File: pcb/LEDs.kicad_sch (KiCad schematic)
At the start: 66 parts, among them U76 74AHCT125

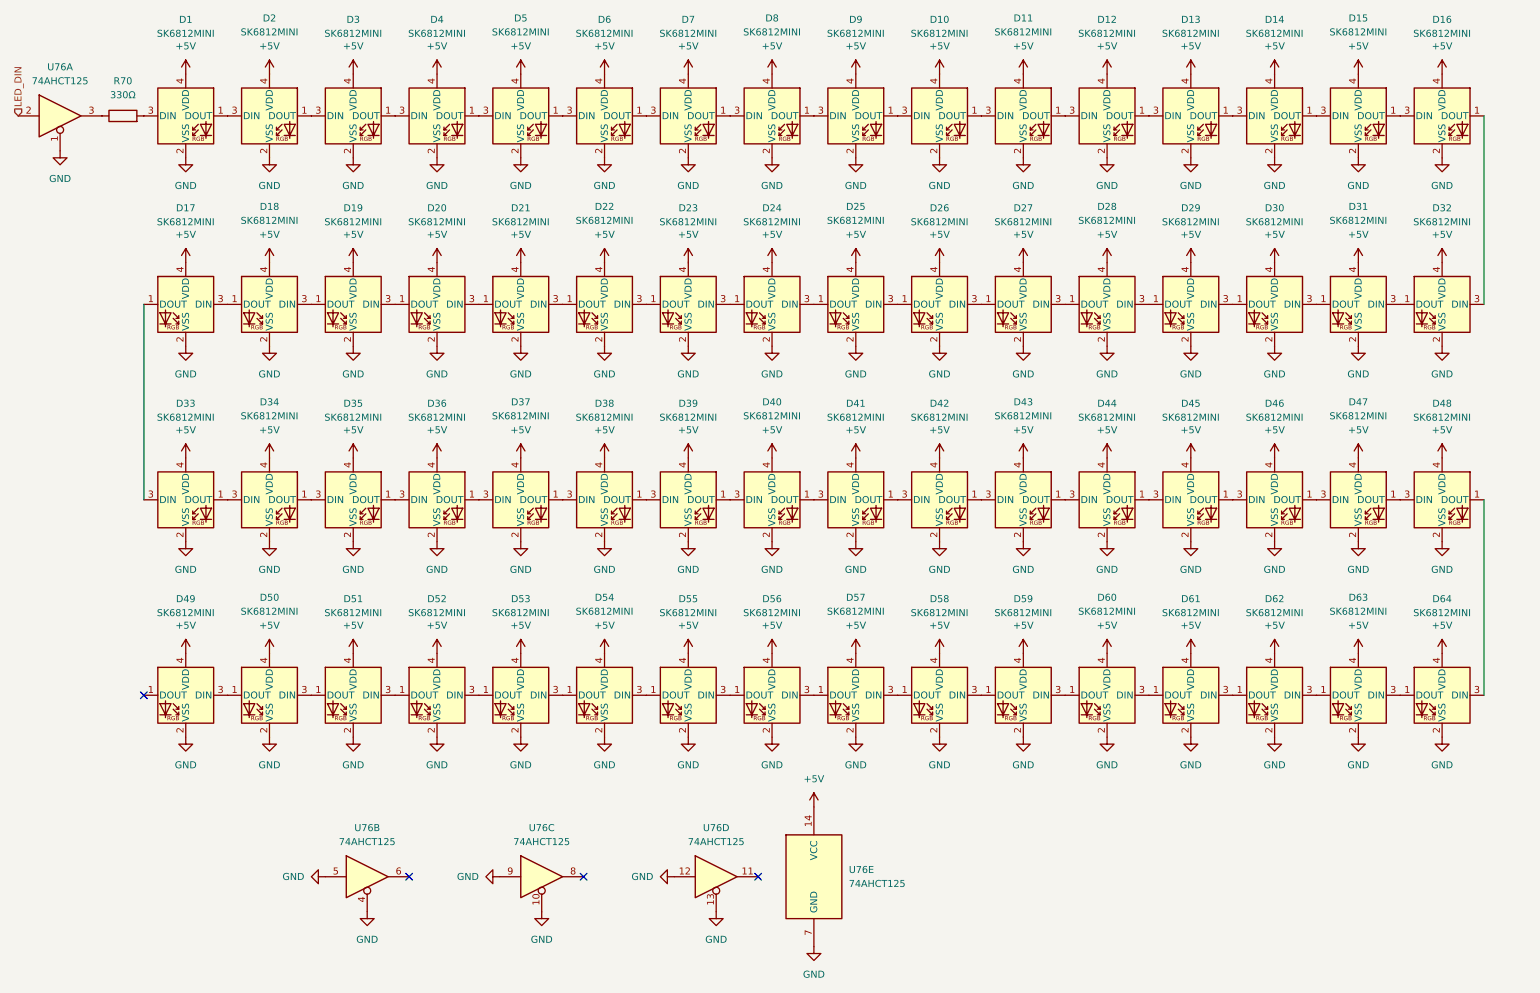
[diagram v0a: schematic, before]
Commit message: feat: completed layout for a single switch
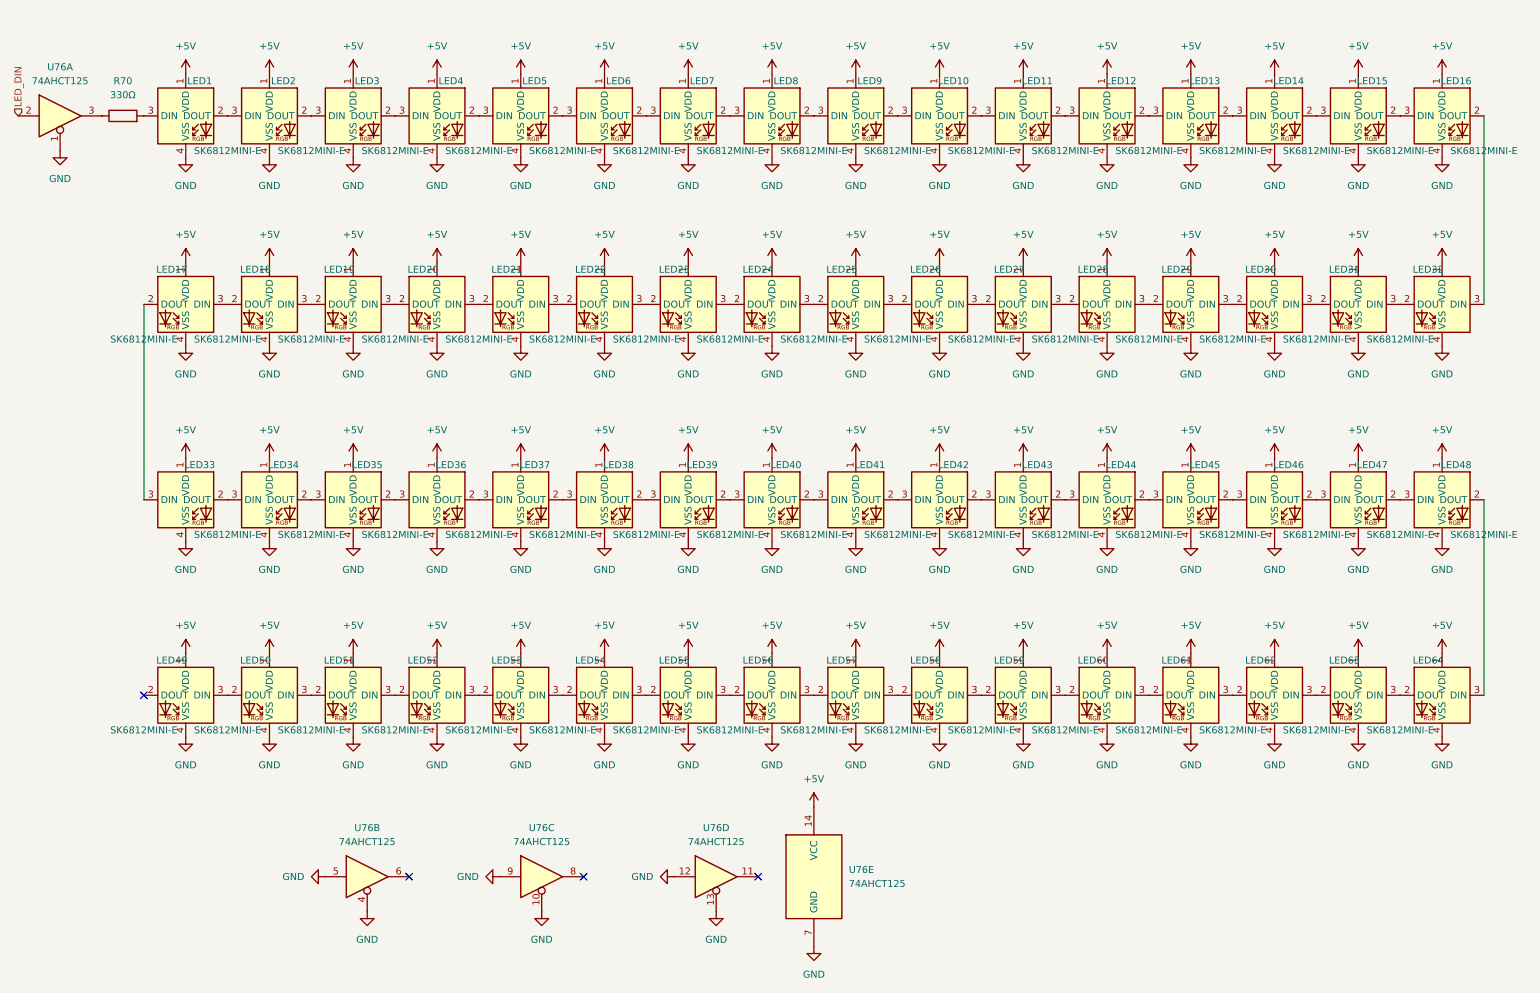
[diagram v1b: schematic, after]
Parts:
- LED1: renamed from D1; value SK6812MINI -> SK6812MINI-E; footprint LED_SMD:LED_SK6812MINI_PLCC4_3.5x3.5mm_P1.75mm -> PCM_marbastlib-various:LED_6028R; symbol LED:SK6812MINI -> PCM_marbastlib-various:SK6812MINI-E
- LED10: renamed from D10; value SK6812MINI -> SK6812MINI-E; footprint LED_SMD:LED_SK6812MINI_PLCC4_3.5x3.5mm_P1.75mm -> PCM_marbastlib-various:LED_6028R; symbol LED:SK6812MINI -> PCM_marbastlib-various:SK6812MINI-E
- LED11: renamed from D11; value SK6812MINI -> SK6812MINI-E; footprint LED_SMD:LED_SK6812MINI_PLCC4_3.5x3.5mm_P1.75mm -> PCM_marbastlib-various:LED_6028R; symbol LED:SK6812MINI -> PCM_marbastlib-various:SK6812MINI-E
- LED12: renamed from D12; value SK6812MINI -> SK6812MINI-E; footprint LED_SMD:LED_SK6812MINI_PLCC4_3.5x3.5mm_P1.75mm -> PCM_marbastlib-various:LED_6028R; symbol LED:SK6812MINI -> PCM_marbastlib-various:SK6812MINI-E
- LED13: renamed from D13; value SK6812MINI -> SK6812MINI-E; footprint LED_SMD:LED_SK6812MINI_PLCC4_3.5x3.5mm_P1.75mm -> PCM_marbastlib-various:LED_6028R; symbol LED:SK6812MINI -> PCM_marbastlib-various:SK6812MINI-E
- LED14: renamed from D14; value SK6812MINI -> SK6812MINI-E; footprint LED_SMD:LED_SK6812MINI_PLCC4_3.5x3.5mm_P1.75mm -> PCM_marbastlib-various:LED_6028R; symbol LED:SK6812MINI -> PCM_marbastlib-various:SK6812MINI-E
- LED15: renamed from D15; value SK6812MINI -> SK6812MINI-E; footprint LED_SMD:LED_SK6812MINI_PLCC4_3.5x3.5mm_P1.75mm -> PCM_marbastlib-various:LED_6028R; symbol LED:SK6812MINI -> PCM_marbastlib-various:SK6812MINI-E
- LED16: renamed from D16; value SK6812MINI -> SK6812MINI-E; footprint LED_SMD:LED_SK6812MINI_PLCC4_3.5x3.5mm_P1.75mm -> PCM_marbastlib-various:LED_6028R; symbol LED:SK6812MINI -> PCM_marbastlib-various:SK6812MINI-E
- LED17: renamed from D17; value SK6812MINI -> SK6812MINI-E; footprint LED_SMD:LED_SK6812MINI_PLCC4_3.5x3.5mm_P1.75mm -> PCM_marbastlib-various:LED_6028R; symbol LED:SK6812MINI -> PCM_marbastlib-various:SK6812MINI-E
- LED18: renamed from D18; value SK6812MINI -> SK6812MINI-E; footprint LED_SMD:LED_SK6812MINI_PLCC4_3.5x3.5mm_P1.75mm -> PCM_marbastlib-various:LED_6028R; symbol LED:SK6812MINI -> PCM_marbastlib-various:SK6812MINI-E
- LED19: renamed from D19; value SK6812MINI -> SK6812MINI-E; footprint LED_SMD:LED_SK6812MINI_PLCC4_3.5x3.5mm_P1.75mm -> PCM_marbastlib-various:LED_6028R; symbol LED:SK6812MINI -> PCM_marbastlib-various:SK6812MINI-E
- LED2: renamed from D2; value SK6812MINI -> SK6812MINI-E; footprint LED_SMD:LED_SK6812MINI_PLCC4_3.5x3.5mm_P1.75mm -> PCM_marbastlib-various:LED_6028R; symbol LED:SK6812MINI -> PCM_marbastlib-various:SK6812MINI-E
- LED20: renamed from D20; value SK6812MINI -> SK6812MINI-E; footprint LED_SMD:LED_SK6812MINI_PLCC4_3.5x3.5mm_P1.75mm -> PCM_marbastlib-various:LED_6028R; symbol LED:SK6812MINI -> PCM_marbastlib-various:SK6812MINI-E
- LED21: renamed from D21; value SK6812MINI -> SK6812MINI-E; footprint LED_SMD:LED_SK6812MINI_PLCC4_3.5x3.5mm_P1.75mm -> PCM_marbastlib-various:LED_6028R; symbol LED:SK6812MINI -> PCM_marbastlib-various:SK6812MINI-E
- LED22: renamed from D22; value SK6812MINI -> SK6812MINI-E; footprint LED_SMD:LED_SK6812MINI_PLCC4_3.5x3.5mm_P1.75mm -> PCM_marbastlib-various:LED_6028R; symbol LED:SK6812MINI -> PCM_marbastlib-various:SK6812MINI-E
- LED23: renamed from D23; value SK6812MINI -> SK6812MINI-E; footprint LED_SMD:LED_SK6812MINI_PLCC4_3.5x3.5mm_P1.75mm -> PCM_marbastlib-various:LED_6028R; symbol LED:SK6812MINI -> PCM_marbastlib-various:SK6812MINI-E
- LED24: renamed from D24; value SK6812MINI -> SK6812MINI-E; footprint LED_SMD:LED_SK6812MINI_PLCC4_3.5x3.5mm_P1.75mm -> PCM_marbastlib-various:LED_6028R; symbol LED:SK6812MINI -> PCM_marbastlib-various:SK6812MINI-E
- LED25: renamed from D25; value SK6812MINI -> SK6812MINI-E; footprint LED_SMD:LED_SK6812MINI_PLCC4_3.5x3.5mm_P1.75mm -> PCM_marbastlib-various:LED_6028R; symbol LED:SK6812MINI -> PCM_marbastlib-various:SK6812MINI-E
- LED26: renamed from D26; value SK6812MINI -> SK6812MINI-E; footprint LED_SMD:LED_SK6812MINI_PLCC4_3.5x3.5mm_P1.75mm -> PCM_marbastlib-various:LED_6028R; symbol LED:SK6812MINI -> PCM_marbastlib-various:SK6812MINI-E
- LED27: renamed from D27; value SK6812MINI -> SK6812MINI-E; footprint LED_SMD:LED_SK6812MINI_PLCC4_3.5x3.5mm_P1.75mm -> PCM_marbastlib-various:LED_6028R; symbol LED:SK6812MINI -> PCM_marbastlib-various:SK6812MINI-E
- LED28: renamed from D28; value SK6812MINI -> SK6812MINI-E; footprint LED_SMD:LED_SK6812MINI_PLCC4_3.5x3.5mm_P1.75mm -> PCM_marbastlib-various:LED_6028R; symbol LED:SK6812MINI -> PCM_marbastlib-various:SK6812MINI-E
- LED29: renamed from D29; value SK6812MINI -> SK6812MINI-E; footprint LED_SMD:LED_SK6812MINI_PLCC4_3.5x3.5mm_P1.75mm -> PCM_marbastlib-various:LED_6028R; symbol LED:SK6812MINI -> PCM_marbastlib-various:SK6812MINI-E
- LED3: renamed from D3; value SK6812MINI -> SK6812MINI-E; footprint LED_SMD:LED_SK6812MINI_PLCC4_3.5x3.5mm_P1.75mm -> PCM_marbastlib-various:LED_6028R; symbol LED:SK6812MINI -> PCM_marbastlib-various:SK6812MINI-E
- LED30: renamed from D30; value SK6812MINI -> SK6812MINI-E; footprint LED_SMD:LED_SK6812MINI_PLCC4_3.5x3.5mm_P1.75mm -> PCM_marbastlib-various:LED_6028R; symbol LED:SK6812MINI -> PCM_marbastlib-various:SK6812MINI-E
- LED31: renamed from D31; value SK6812MINI -> SK6812MINI-E; footprint LED_SMD:LED_SK6812MINI_PLCC4_3.5x3.5mm_P1.75mm -> PCM_marbastlib-various:LED_6028R; symbol LED:SK6812MINI -> PCM_marbastlib-various:SK6812MINI-E
- LED32: renamed from D32; value SK6812MINI -> SK6812MINI-E; footprint LED_SMD:LED_SK6812MINI_PLCC4_3.5x3.5mm_P1.75mm -> PCM_marbastlib-various:LED_6028R; symbol LED:SK6812MINI -> PCM_marbastlib-various:SK6812MINI-E
- LED33: renamed from D33; value SK6812MINI -> SK6812MINI-E; footprint LED_SMD:LED_SK6812MINI_PLCC4_3.5x3.5mm_P1.75mm -> PCM_marbastlib-various:LED_6028R; symbol LED:SK6812MINI -> PCM_marbastlib-various:SK6812MINI-E
- LED34: renamed from D34; value SK6812MINI -> SK6812MINI-E; footprint LED_SMD:LED_SK6812MINI_PLCC4_3.5x3.5mm_P1.75mm -> PCM_marbastlib-various:LED_6028R; symbol LED:SK6812MINI -> PCM_marbastlib-various:SK6812MINI-E
- LED35: renamed from D35; value SK6812MINI -> SK6812MINI-E; footprint LED_SMD:LED_SK6812MINI_PLCC4_3.5x3.5mm_P1.75mm -> PCM_marbastlib-various:LED_6028R; symbol LED:SK6812MINI -> PCM_marbastlib-various:SK6812MINI-E
- LED36: renamed from D36; value SK6812MINI -> SK6812MINI-E; footprint LED_SMD:LED_SK6812MINI_PLCC4_3.5x3.5mm_P1.75mm -> PCM_marbastlib-various:LED_6028R; symbol LED:SK6812MINI -> PCM_marbastlib-various:SK6812MINI-E
- LED37: renamed from D37; value SK6812MINI -> SK6812MINI-E; footprint LED_SMD:LED_SK6812MINI_PLCC4_3.5x3.5mm_P1.75mm -> PCM_marbastlib-various:LED_6028R; symbol LED:SK6812MINI -> PCM_marbastlib-various:SK6812MINI-E
- LED38: renamed from D38; value SK6812MINI -> SK6812MINI-E; footprint LED_SMD:LED_SK6812MINI_PLCC4_3.5x3.5mm_P1.75mm -> PCM_marbastlib-various:LED_6028R; symbol LED:SK6812MINI -> PCM_marbastlib-various:SK6812MINI-E
- LED39: renamed from D39; value SK6812MINI -> SK6812MINI-E; footprint LED_SMD:LED_SK6812MINI_PLCC4_3.5x3.5mm_P1.75mm -> PCM_marbastlib-various:LED_6028R; symbol LED:SK6812MINI -> PCM_marbastlib-various:SK6812MINI-E
- LED4: renamed from D4; value SK6812MINI -> SK6812MINI-E; footprint LED_SMD:LED_SK6812MINI_PLCC4_3.5x3.5mm_P1.75mm -> PCM_marbastlib-various:LED_6028R; symbol LED:SK6812MINI -> PCM_marbastlib-various:SK6812MINI-E
- LED40: renamed from D40; value SK6812MINI -> SK6812MINI-E; footprint LED_SMD:LED_SK6812MINI_PLCC4_3.5x3.5mm_P1.75mm -> PCM_marbastlib-various:LED_6028R; symbol LED:SK6812MINI -> PCM_marbastlib-various:SK6812MINI-E
- LED41: renamed from D41; value SK6812MINI -> SK6812MINI-E; footprint LED_SMD:LED_SK6812MINI_PLCC4_3.5x3.5mm_P1.75mm -> PCM_marbastlib-various:LED_6028R; symbol LED:SK6812MINI -> PCM_marbastlib-various:SK6812MINI-E
- LED42: renamed from D42; value SK6812MINI -> SK6812MINI-E; footprint LED_SMD:LED_SK6812MINI_PLCC4_3.5x3.5mm_P1.75mm -> PCM_marbastlib-various:LED_6028R; symbol LED:SK6812MINI -> PCM_marbastlib-various:SK6812MINI-E
- LED43: renamed from D43; value SK6812MINI -> SK6812MINI-E; footprint LED_SMD:LED_SK6812MINI_PLCC4_3.5x3.5mm_P1.75mm -> PCM_marbastlib-various:LED_6028R; symbol LED:SK6812MINI -> PCM_marbastlib-various:SK6812MINI-E
- LED44: renamed from D44; value SK6812MINI -> SK6812MINI-E; footprint LED_SMD:LED_SK6812MINI_PLCC4_3.5x3.5mm_P1.75mm -> PCM_marbastlib-various:LED_6028R; symbol LED:SK6812MINI -> PCM_marbastlib-various:SK6812MINI-E
- LED45: renamed from D45; value SK6812MINI -> SK6812MINI-E; footprint LED_SMD:LED_SK6812MINI_PLCC4_3.5x3.5mm_P1.75mm -> PCM_marbastlib-various:LED_6028R; symbol LED:SK6812MINI -> PCM_marbastlib-various:SK6812MINI-E
- LED46: renamed from D46; value SK6812MINI -> SK6812MINI-E; footprint LED_SMD:LED_SK6812MINI_PLCC4_3.5x3.5mm_P1.75mm -> PCM_marbastlib-various:LED_6028R; symbol LED:SK6812MINI -> PCM_marbastlib-various:SK6812MINI-E
- LED47: renamed from D47; value SK6812MINI -> SK6812MINI-E; footprint LED_SMD:LED_SK6812MINI_PLCC4_3.5x3.5mm_P1.75mm -> PCM_marbastlib-various:LED_6028R; symbol LED:SK6812MINI -> PCM_marbastlib-various:SK6812MINI-E
- LED48: renamed from D48; value SK6812MINI -> SK6812MINI-E; footprint LED_SMD:LED_SK6812MINI_PLCC4_3.5x3.5mm_P1.75mm -> PCM_marbastlib-various:LED_6028R; symbol LED:SK6812MINI -> PCM_marbastlib-various:SK6812MINI-E
- LED49: renamed from D49; value SK6812MINI -> SK6812MINI-E; footprint LED_SMD:LED_SK6812MINI_PLCC4_3.5x3.5mm_P1.75mm -> PCM_marbastlib-various:LED_6028R; symbol LED:SK6812MINI -> PCM_marbastlib-various:SK6812MINI-E
- LED5: renamed from D5; value SK6812MINI -> SK6812MINI-E; footprint LED_SMD:LED_SK6812MINI_PLCC4_3.5x3.5mm_P1.75mm -> PCM_marbastlib-various:LED_6028R; symbol LED:SK6812MINI -> PCM_marbastlib-various:SK6812MINI-E
- LED50: renamed from D50; value SK6812MINI -> SK6812MINI-E; footprint LED_SMD:LED_SK6812MINI_PLCC4_3.5x3.5mm_P1.75mm -> PCM_marbastlib-various:LED_6028R; symbol LED:SK6812MINI -> PCM_marbastlib-various:SK6812MINI-E
- LED51: renamed from D51; value SK6812MINI -> SK6812MINI-E; footprint LED_SMD:LED_SK6812MINI_PLCC4_3.5x3.5mm_P1.75mm -> PCM_marbastlib-various:LED_6028R; symbol LED:SK6812MINI -> PCM_marbastlib-various:SK6812MINI-E
- LED52: renamed from D52; value SK6812MINI -> SK6812MINI-E; footprint LED_SMD:LED_SK6812MINI_PLCC4_3.5x3.5mm_P1.75mm -> PCM_marbastlib-various:LED_6028R; symbol LED:SK6812MINI -> PCM_marbastlib-various:SK6812MINI-E
- LED53: renamed from D53; value SK6812MINI -> SK6812MINI-E; footprint LED_SMD:LED_SK6812MINI_PLCC4_3.5x3.5mm_P1.75mm -> PCM_marbastlib-various:LED_6028R; symbol LED:SK6812MINI -> PCM_marbastlib-various:SK6812MINI-E
- LED54: renamed from D54; value SK6812MINI -> SK6812MINI-E; footprint LED_SMD:LED_SK6812MINI_PLCC4_3.5x3.5mm_P1.75mm -> PCM_marbastlib-various:LED_6028R; symbol LED:SK6812MINI -> PCM_marbastlib-various:SK6812MINI-E
- LED55: renamed from D55; value SK6812MINI -> SK6812MINI-E; footprint LED_SMD:LED_SK6812MINI_PLCC4_3.5x3.5mm_P1.75mm -> PCM_marbastlib-various:LED_6028R; symbol LED:SK6812MINI -> PCM_marbastlib-various:SK6812MINI-E
- LED56: renamed from D56; value SK6812MINI -> SK6812MINI-E; footprint LED_SMD:LED_SK6812MINI_PLCC4_3.5x3.5mm_P1.75mm -> PCM_marbastlib-various:LED_6028R; symbol LED:SK6812MINI -> PCM_marbastlib-various:SK6812MINI-E
- LED57: renamed from D57; value SK6812MINI -> SK6812MINI-E; footprint LED_SMD:LED_SK6812MINI_PLCC4_3.5x3.5mm_P1.75mm -> PCM_marbastlib-various:LED_6028R; symbol LED:SK6812MINI -> PCM_marbastlib-various:SK6812MINI-E
- LED58: renamed from D58; value SK6812MINI -> SK6812MINI-E; footprint LED_SMD:LED_SK6812MINI_PLCC4_3.5x3.5mm_P1.75mm -> PCM_marbastlib-various:LED_6028R; symbol LED:SK6812MINI -> PCM_marbastlib-various:SK6812MINI-E
- LED59: renamed from D59; value SK6812MINI -> SK6812MINI-E; footprint LED_SMD:LED_SK6812MINI_PLCC4_3.5x3.5mm_P1.75mm -> PCM_marbastlib-various:LED_6028R; symbol LED:SK6812MINI -> PCM_marbastlib-various:SK6812MINI-E
- LED6: renamed from D6; value SK6812MINI -> SK6812MINI-E; footprint LED_SMD:LED_SK6812MINI_PLCC4_3.5x3.5mm_P1.75mm -> PCM_marbastlib-various:LED_6028R; symbol LED:SK6812MINI -> PCM_marbastlib-various:SK6812MINI-E
- LED60: renamed from D60; value SK6812MINI -> SK6812MINI-E; footprint LED_SMD:LED_SK6812MINI_PLCC4_3.5x3.5mm_P1.75mm -> PCM_marbastlib-various:LED_6028R; symbol LED:SK6812MINI -> PCM_marbastlib-various:SK6812MINI-E
- LED61: renamed from D61; value SK6812MINI -> SK6812MINI-E; footprint LED_SMD:LED_SK6812MINI_PLCC4_3.5x3.5mm_P1.75mm -> PCM_marbastlib-various:LED_6028R; symbol LED:SK6812MINI -> PCM_marbastlib-various:SK6812MINI-E
- LED62: renamed from D62; value SK6812MINI -> SK6812MINI-E; footprint LED_SMD:LED_SK6812MINI_PLCC4_3.5x3.5mm_P1.75mm -> PCM_marbastlib-various:LED_6028R; symbol LED:SK6812MINI -> PCM_marbastlib-various:SK6812MINI-E
- LED63: renamed from D63; value SK6812MINI -> SK6812MINI-E; footprint LED_SMD:LED_SK6812MINI_PLCC4_3.5x3.5mm_P1.75mm -> PCM_marbastlib-various:LED_6028R; symbol LED:SK6812MINI -> PCM_marbastlib-various:SK6812MINI-E
- LED64: renamed from D64; value SK6812MINI -> SK6812MINI-E; footprint LED_SMD:LED_SK6812MINI_PLCC4_3.5x3.5mm_P1.75mm -> PCM_marbastlib-various:LED_6028R; symbol LED:SK6812MINI -> PCM_marbastlib-various:SK6812MINI-E
- LED7: renamed from D7; value SK6812MINI -> SK6812MINI-E; footprint LED_SMD:LED_SK6812MINI_PLCC4_3.5x3.5mm_P1.75mm -> PCM_marbastlib-various:LED_6028R; symbol LED:SK6812MINI -> PCM_marbastlib-various:SK6812MINI-E
- LED8: renamed from D8; value SK6812MINI -> SK6812MINI-E; footprint LED_SMD:LED_SK6812MINI_PLCC4_3.5x3.5mm_P1.75mm -> PCM_marbastlib-various:LED_6028R; symbol LED:SK6812MINI -> PCM_marbastlib-various:SK6812MINI-E
- LED9: renamed from D9; value SK6812MINI -> SK6812MINI-E; footprint LED_SMD:LED_SK6812MINI_PLCC4_3.5x3.5mm_P1.75mm -> PCM_marbastlib-various:LED_6028R; symbol LED:SK6812MINI -> PCM_marbastlib-various:SK6812MINI-E
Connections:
- net +5V: now also LED1.1 (VDD), LED10.1 (VDD), LED11.1 (VDD), LED12.1 (VDD), LED13.1 (VDD), LED14.1 (VDD), LED15.1 (VDD), LED16.1 (VDD), LED17.1 (VDD), LED18.1 (VDD), LED19.1 (VDD), LED2.1 (VDD), LED20.1 (VDD), LED21.1 (VDD), LED22.1 (VDD), LED23.1 (VDD), LED24.1 (VDD), LED25.1 (VDD), LED26.1 (VDD), LED27.1 (VDD), LED28.1 (VDD), LED29.1 (VDD), LED3.1 (VDD), LED30.1 (VDD), LED31.1 (VDD), LED32.1 (VDD), LED33.1 (VDD), LED34.1 (VDD), LED35.1 (VDD), LED36.1 (VDD), LED37.1 (VDD), LED38.1 (VDD), LED39.1 (VDD), LED4.1 (VDD), LED40.1 (VDD), LED41.1 (VDD), LED42.1 (VDD), LED43.1 (VDD), LED44.1 (VDD), LED45.1 (VDD), LED46.1 (VDD), LED47.1 (VDD), LED48.1 (VDD), LED49.1 (VDD), LED5.1 (VDD), LED50.1 (VDD), LED51.1 (VDD), LED52.1 (VDD), LED53.1 (VDD), LED54.1 (VDD), LED55.1 (VDD), LED56.1 (VDD), LED57.1 (VDD), LED58.1 (VDD), LED59.1 (VDD), LED6.1 (VDD), LED60.1 (VDD), LED61.1 (VDD), LED62.1 (VDD), LED63.1 (VDD), LED64.1 (VDD), LED7.1 (VDD), LED8.1 (VDD), LED9.1 (VDD); no longer LED1.4 (VDD), LED10.4 (VDD), LED11.4 (VDD), LED12.4 (VDD), LED13.4 (VDD), LED14.4 (VDD), LED15.4 (VDD), LED16.4 (VDD), LED17.4 (VDD), LED18.4 (VDD), LED19.4 (VDD), LED2.4 (VDD), LED20.4 (VDD), LED21.4 (VDD), LED22.4 (VDD), LED23.4 (VDD), LED24.4 (VDD), LED25.4 (VDD), LED26.4 (VDD), LED27.4 (VDD), LED28.4 (VDD), LED29.4 (VDD), LED3.4 (VDD), LED30.4 (VDD), LED31.4 (VDD), LED32.4 (VDD), LED33.4 (VDD), LED34.4 (VDD), LED35.4 (VDD), LED36.4 (VDD), LED37.4 (VDD), LED38.4 (VDD), LED39.4 (VDD), LED4.4 (VDD), LED40.4 (VDD), LED41.4 (VDD), LED42.4 (VDD), LED43.4 (VDD), LED44.4 (VDD), LED45.4 (VDD), LED46.4 (VDD), LED47.4 (VDD), LED48.4 (VDD), LED49.4 (VDD), LED5.4 (VDD), LED50.4 (VDD), LED51.4 (VDD), LED52.4 (VDD), LED53.4 (VDD), LED54.4 (VDD), LED55.4 (VDD), LED56.4 (VDD), LED57.4 (VDD), LED58.4 (VDD), LED59.4 (VDD), LED6.4 (VDD), LED60.4 (VDD), LED61.4 (VDD), LED62.4 (VDD), LED63.4 (VDD), LED64.4 (VDD), LED7.4 (VDD), LED8.4 (VDD), LED9.4 (VDD)
- net GND: now also LED1.4 (VSS), LED10.4 (VSS), LED11.4 (VSS), LED12.4 (VSS), LED13.4 (VSS), LED14.4 (VSS), LED15.4 (VSS), LED16.4 (VSS), LED17.4 (VSS), LED18.4 (VSS), LED19.4 (VSS), LED2.4 (VSS), LED20.4 (VSS), LED21.4 (VSS), LED22.4 (VSS), LED23.4 (VSS), LED24.4 (VSS), LED25.4 (VSS), LED26.4 (VSS), LED27.4 (VSS), LED28.4 (VSS), LED29.4 (VSS), LED3.4 (VSS), LED30.4 (VSS), LED31.4 (VSS), LED32.4 (VSS), LED33.4 (VSS), LED34.4 (VSS), LED35.4 (VSS), LED36.4 (VSS), LED37.4 (VSS), LED38.4 (VSS), LED39.4 (VSS), LED4.4 (VSS), LED40.4 (VSS), LED41.4 (VSS), LED42.4 (VSS), LED43.4 (VSS), LED44.4 (VSS), LED45.4 (VSS), LED46.4 (VSS), LED47.4 (VSS), LED48.4 (VSS), LED49.4 (VSS), LED5.4 (VSS), LED50.4 (VSS), LED51.4 (VSS), LED52.4 (VSS), LED53.4 (VSS), LED54.4 (VSS), LED55.4 (VSS), LED56.4 (VSS), LED57.4 (VSS), LED58.4 (VSS), LED59.4 (VSS), LED6.4 (VSS), LED60.4 (VSS), LED61.4 (VSS), LED62.4 (VSS), LED63.4 (VSS), LED64.4 (VSS), LED7.4 (VSS), LED8.4 (VSS), LED9.4 (VSS); no longer LED1.2 (VSS), LED10.2 (VSS), LED11.2 (VSS), LED12.2 (VSS), LED13.2 (VSS), LED14.2 (VSS), LED15.2 (VSS), LED16.2 (VSS), LED17.2 (VSS), LED18.2 (VSS), LED19.2 (VSS), LED2.2 (VSS), LED20.2 (VSS), LED21.2 (VSS), LED22.2 (VSS), LED23.2 (VSS), LED24.2 (VSS), LED25.2 (VSS), LED26.2 (VSS), LED27.2 (VSS), LED28.2 (VSS), LED29.2 (VSS), LED3.2 (VSS), LED30.2 (VSS), LED31.2 (VSS), LED32.2 (VSS), LED33.2 (VSS), LED34.2 (VSS), LED35.2 (VSS), LED36.2 (VSS), LED37.2 (VSS), LED38.2 (VSS), LED39.2 (VSS), LED4.2 (VSS), LED40.2 (VSS), LED41.2 (VSS), LED42.2 (VSS), LED43.2 (VSS), LED44.2 (VSS), LED45.2 (VSS), LED46.2 (VSS), LED47.2 (VSS), LED48.2 (VSS), LED49.2 (VSS), LED5.2 (VSS), LED50.2 (VSS), LED51.2 (VSS), LED52.2 (VSS), LED53.2 (VSS), LED54.2 (VSS), LED55.2 (VSS), LED56.2 (VSS), LED57.2 (VSS), LED58.2 (VSS), LED59.2 (VSS), LED6.2 (VSS), LED60.2 (VSS), LED61.2 (VSS), LED62.2 (VSS), LED63.2 (VSS), LED64.2 (VSS), LED7.2 (VSS), LED8.2 (VSS), LED9.2 (VSS)
- net at LED4.3 (DIN): now also LED3.2 (DOUT); no longer LED3.1 (DOUT)
- net at LED3.3 (DIN): now also LED2.2 (DOUT); no longer LED2.1 (DOUT)
- net at LED49.3 (DIN): now also LED50.2 (DOUT); no longer LED50.1 (DOUT)
- net at LED50.3 (DIN): now also LED51.2 (DOUT); no longer LED51.1 (DOUT)
- net at LED8.3 (DIN): now also LED7.2 (DOUT); no longer LED7.1 (DOUT)
- net at LED7.3 (DIN): now also LED6.2 (DOUT); no longer LED6.1 (DOUT)
- net at LED64.3 (DIN): now also LED48.2 (DOUT); no longer LED48.1 (DOUT)
- net at LED48.3 (DIN): now also LED47.2 (DOUT); no longer LED47.1 (DOUT)
- net at LED6.3 (DIN): now also LED5.2 (DOUT); no longer LED5.1 (DOUT)
- net at LED5.3 (DIN): now also LED4.2 (DOUT); no longer LED4.1 (DOUT)
- net at LED56.3 (DIN): now also LED57.2 (DOUT); no longer LED57.1 (DOUT)
- net at LED57.3 (DIN): now also LED58.2 (DOUT); no longer LED58.1 (DOUT)
- net at LED28.3 (DIN): now also LED29.2 (DOUT); no longer LED29.1 (DOUT)
- net at LED29.3 (DIN): now also LED30.2 (DOUT); no longer LED30.1 (DOUT)
- net at LED61.3 (DIN): now also LED62.2 (DOUT); no longer LED62.1 (DOUT)
- net at LED62.3 (DIN): now also LED63.2 (DOUT); no longer LED63.1 (DOUT)
- net at LED42.3 (DIN): now also LED41.2 (DOUT); no longer LED41.1 (DOUT)
- net at LED41.3 (DIN): now also LED40.2 (DOUT); no longer LED40.1 (DOUT)
- net at LED2.3 (DIN): now also LED1.2 (DOUT); no longer LED1.1 (DOUT)
- net at LED18.3 (DIN): now also LED19.2 (DOUT); no longer LED19.1 (DOUT)
- net at LED19.3 (DIN): now also LED20.2 (DOUT); no longer LED20.1 (DOUT)
- net at LED55.3 (DIN): now also LED56.2 (DOUT); no longer LED56.1 (DOUT)
- net at LED12.3 (DIN): now also LED11.2 (DOUT); no longer LED11.1 (DOUT)
- net at LED11.3 (DIN): now also LED10.2 (DOUT); no longer LED10.1 (DOUT)
- net at LED47.3 (DIN): now also LED46.2 (DOUT); no longer LED46.1 (DOUT)
- net at LED17.3 (DIN): now also LED18.2 (DOUT); no longer LED18.1 (DOUT)
- net at LED30.3 (DIN): now also LED31.2 (DOUT); no longer LED31.1 (DOUT)
- net at LED38.3 (DIN): now also LED37.2 (DOUT); no longer LED37.1 (DOUT)
- net at LED37.3 (DIN): now also LED36.2 (DOUT); no longer LED36.1 (DOUT)
- net at LED53.3 (DIN): now also LED54.2 (DOUT); no longer LED54.1 (DOUT)
- net at LED54.3 (DIN): now also LED55.2 (DOUT); no longer LED55.1 (DOUT)
- net at LED60.3 (DIN): now also LED61.2 (DOUT); no longer LED61.1 (DOUT)
- net at LED32.3 (DIN): now also LED16.2 (DOUT); no longer LED16.1 (DOUT)
- net at LED16.3 (DIN): now also LED15.2 (DOUT); no longer LED15.1 (DOUT)
- net at LED51.3 (DIN): now also LED52.2 (DOUT); no longer LED52.1 (DOUT)
- net at LED52.3 (DIN): now also LED53.2 (DOUT); no longer LED53.1 (DOUT)
- net at LED25.3 (DIN): now also LED26.2 (DOUT); no longer LED26.1 (DOUT)
- net at LED26.3 (DIN): now also LED27.2 (DOUT); no longer LED27.1 (DOUT)
- net at LED27.3 (DIN): now also LED28.2 (DOUT); no longer LED28.1 (DOUT)
- net at LED20.3 (DIN): now also LED21.2 (DOUT); no longer LED21.1 (DOUT)
- net at LED21.3 (DIN): now also LED22.2 (DOUT); no longer LED22.1 (DOUT)
- net at LED39.3 (DIN): now also LED38.2 (DOUT); no longer LED38.1 (DOUT)
- net at LED58.3 (DIN): now also LED59.2 (DOUT); no longer LED59.1 (DOUT)
- net at LED9.3 (DIN): now also LED8.2 (DOUT); no longer LED8.1 (DOUT)
- net at LED15.3 (DIN): now also LED14.2 (DOUT); no longer LED14.1 (DOUT)
- net at LED59.3 (DIN): now also LED60.2 (DOUT); no longer LED60.1 (DOUT)
- net at LED46.3 (DIN): now also LED45.2 (DOUT); no longer LED45.1 (DOUT)
- net at LED45.3 (DIN): now also LED44.2 (DOUT); no longer LED44.1 (DOUT)
- net at LED36.3 (DIN): now also LED35.2 (DOUT); no longer LED35.1 (DOUT)
- net at LED35.3 (DIN): now also LED34.2 (DOUT); no longer LED34.1 (DOUT)
- net at LED23.3 (DIN): now also LED24.2 (DOUT); no longer LED24.1 (DOUT)
- net at LED24.3 (DIN): now also LED25.2 (DOUT); no longer LED25.1 (DOUT)
- net at LED22.3 (DIN): now also LED23.2 (DOUT); no longer LED23.1 (DOUT)
- net at LED63.3 (DIN): now also LED64.2 (DOUT); no longer LED64.1 (DOUT)
- net at LED43.3 (DIN): now also LED42.2 (DOUT); no longer LED42.1 (DOUT)
- net at LED40.3 (DIN): now also LED39.2 (DOUT); no longer LED39.1 (DOUT)
- net at LED14.3 (DIN): now also LED13.2 (DOUT); no longer LED13.1 (DOUT)
- net at LED44.3 (DIN): now also LED43.2 (DOUT); no longer LED43.1 (DOUT)
- net at LED33.3 (DIN): now also LED17.2 (DOUT); no longer LED17.1 (DOUT)
- net at LED31.3 (DIN): now also LED32.2 (DOUT); no longer LED32.1 (DOUT)
- net at LED13.3 (DIN): now also LED12.2 (DOUT); no longer LED12.1 (DOUT)
- net at LED34.3 (DIN): now also LED33.2 (DOUT); no longer LED33.1 (DOUT)
- net at LED10.3 (DIN): now also LED9.2 (DOUT); no longer LED9.1 (DOUT)
